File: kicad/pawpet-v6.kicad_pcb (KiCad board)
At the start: 2 copper layers, 51.8 x 51.8 mm, 39 parts, among them J1 USB4105-GF-A, J2 Conn_ARM_JTAG_SWD_10, J3 MOLEX, U1 ATSAMD21G18A-A, U2 TPS61261DRVT, U3 MX25R1635FM1IL0, Y1 32,768

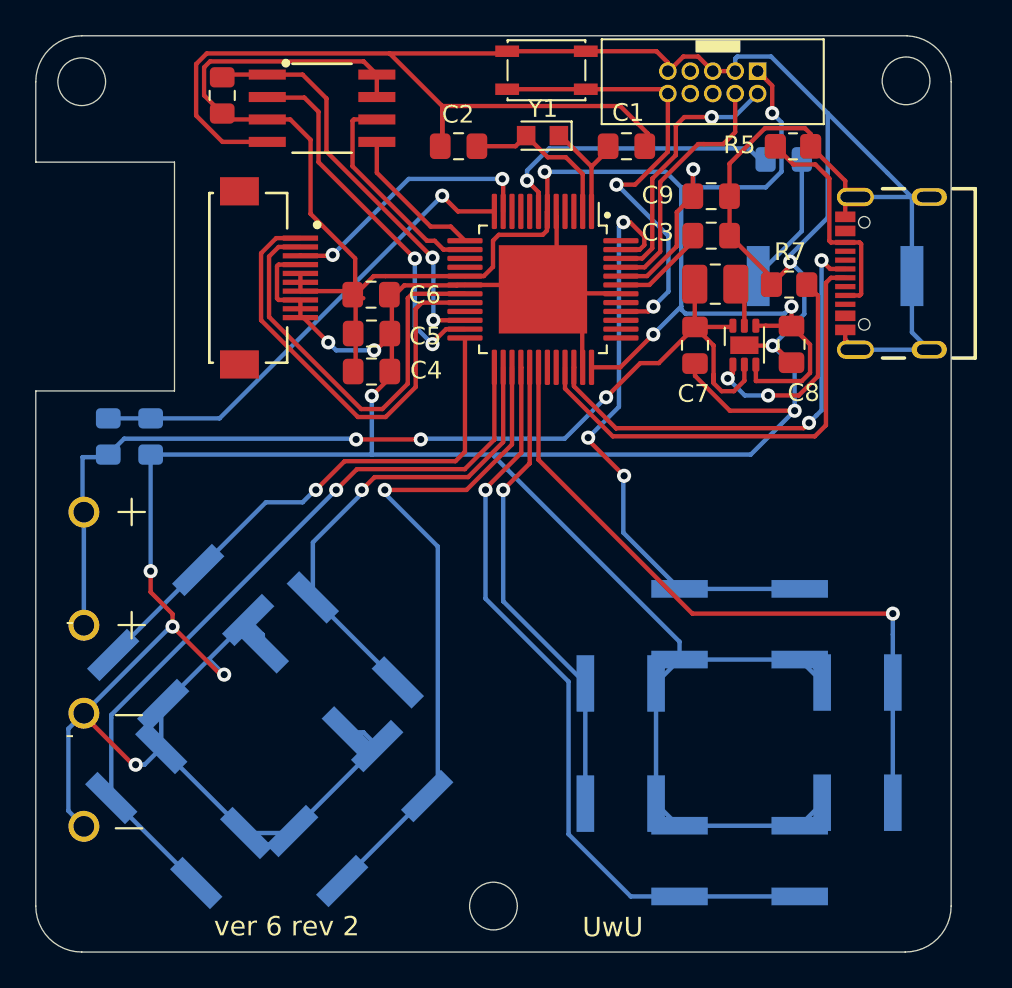
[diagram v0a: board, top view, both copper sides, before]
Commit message: power opt tests
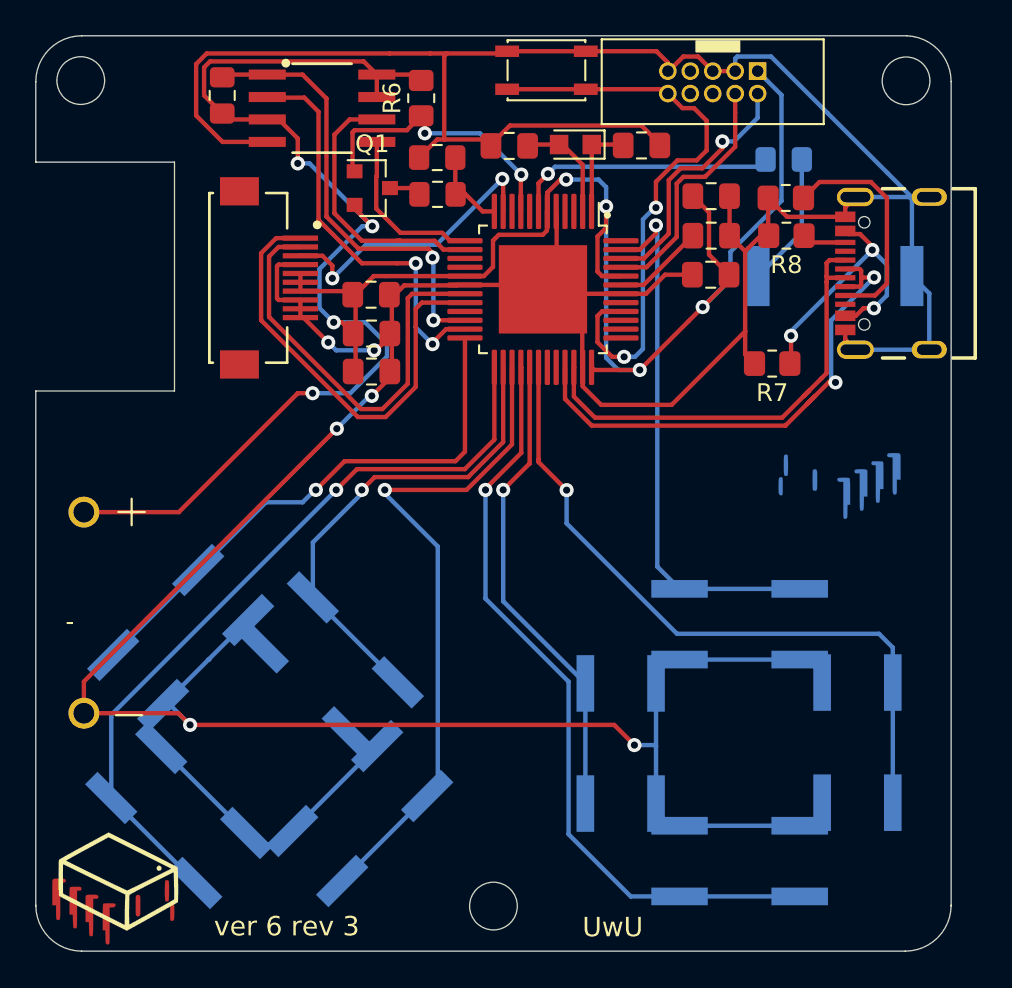
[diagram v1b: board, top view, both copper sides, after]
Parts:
- removed the BT1 at (157.2, 103.0)
- removed C7: 10uF, Capacitor_SMD:C_0805_2012Metric_Pad1.18x1.45mm_HandSolder
- removed L1: L_Small, Inductor_SMD:L_1008_2520Metric_Pad1.43x2.20mm_HandSolder
- removed U2: TPS61261DRVT, pawpet:WSON-6-1EP_2x2mm_P0.65mm_EP1x1.6mm_custom
- added Q1: DMG2301L, Package_TO_SOT_SMD:SOT-23, F.Cu at (150.3, 72.6)
- added R6: 100k, Resistor_SMD:R_0805_2012Metric_Pad1.20x1.40mm_HandSolder, F.Cu at (153.1, 67.5)
- added R8: 5.1k, Resistor_SMD:R_0805_2012Metric_Pad1.20x1.40mm_HandSolder, F.Cu at (173.8, 75.3)
- added Ref**: Val**, pawpet:kicad-drawing, B.Cu at (177.8, 88.6)
- added Ref**: Val**, pawpet:kicad-drawing, F.Cu at (134.7, 112.7)
- R1: value 10k -> 100k
- R2: value 470 -> 1k
- R3, R4: moved to F.Cu
- R7: value 20k -> 1k
- moved R3 23.1 mm to (154.0, 73.0), turned to 180 degrees
- moved R4 22.6 mm to (154.0, 70.9), turned to 0 degrees
- moved C8 6.04 mm to (169.5, 77.5), turned to 180 degrees
- moved R7 4.57 mm to (173.0, 82.5)
- moved R5 2.95 mm to (173.7, 73.2), turned to 180 degrees
- moved C2 2.87 mm to (158.1, 70.2)
- moved Y1 1.93 mm to (161.8, 70.2)
- moved C1 0.85 mm to (165.6, 70.2)
- moved REF** 0.08 mm to (133.8, 66.5)
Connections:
- BT1 pad 1: Net-(BT1-Pad1) -> +3V3
- J1 pad A6: /D- -> /D+
- J1 pad A7: /D+ -> /D-
- J1 pad B4_A9: Net-(J1-PadB4_A9) -> Net-(J1-PadA4_B9)
- J1 pad B5: Net-(J1-PadA5) -> Net-(J1-PadB5)
- J1 pad B6: Net-(J1-PadB6) -> /D+
- J1 pad B7: Net-(J1-PadB7) -> /D-
- R3 pad 2: Net-(BT1-Pad1) -> Net-(Q1-Pad3)
- R7 pad 1: Net-(R7-Pad1) -> Net-(J1-PadA4_B9)
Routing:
- net Net-(BT1-Pad1): track 59.0 -> 0.00 mm, vias 3 -> 0
- net GND: track 336.6 -> 292.5 mm, vias 10 -> 6
- net +3V3: track 116.0 -> 140.6 mm, vias 5 -> 8
- net /A7: track 27.4 -> 4.35 mm, vias 1 -> 0
- net Net-(J1-PadA4_B9): track 0.00 -> 16.4 mm, vias 0 -> 3
- net /A3: track 0.00 -> 16.1 mm, vias 0 -> 2
- net Net-(R7-Pad1): track 12.6 -> 0.00 mm, vias 2 -> 0
- net /reset: track 27.0 -> 33.5 mm
- net /FLASH_SCK: track 12.3 -> 16.4 mm
- net Net-(C2-Pad2): track 9.52 -> 6.23 mm
- net /A5: track 34.1 -> 30.8 mm, vias 3 -> 1
- net /D-: track 26.6 -> 29.8 mm, vias 0 -> 2
- net Net-(L1-Pad2): track 2.55 -> 0.00 mm
- net Net-(J1-PadB5): track 0.00 -> 2.49 mm
- net /FLASH_CS: track 23.4 -> 25.7 mm
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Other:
- board text added: "ver 6 rev 3"
- board text removed: "ver 6 rev 2"
